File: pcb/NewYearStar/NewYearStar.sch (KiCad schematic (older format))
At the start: 22 parts, among them J1 Conn_01x03_Male, J2 Conn_01x02_Male, J3 Conn_01x02_Male, J4 Conn_01x02_Male, J5 Conn_01x02_Male

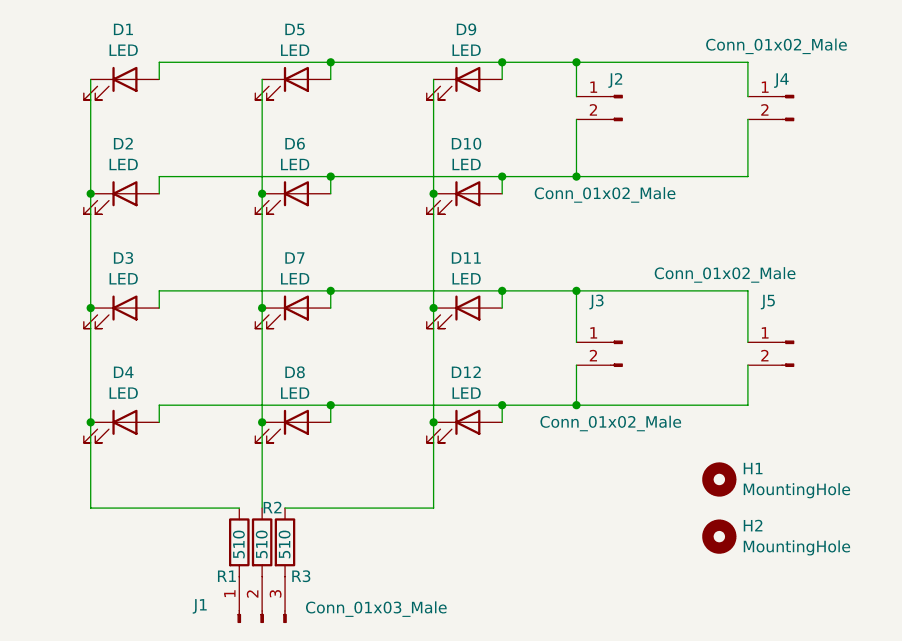
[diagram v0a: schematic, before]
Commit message: Add R for every LED
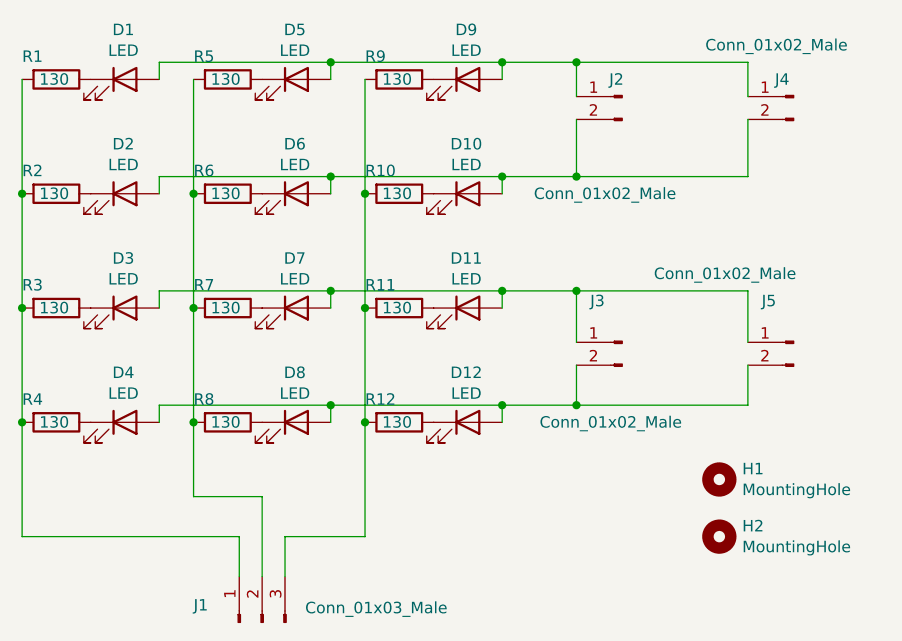
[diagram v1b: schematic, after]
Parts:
- added R10, R11, R12, R4, R5, R6, R7, R8, R9: 130, Resistor_SMD:R_0805_2012Metric_Pad1.20x1.40mm_HandSolder, symbol Device:R
- R1, R2, R3: value 510 -> 130
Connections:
- net at J1.1 (Pin_1), R1.2: now also R2.2, R3.2, R4.2
- net at J1.2 (Pin_2): now also R5.2, R6.2, R7.2, R8.2; no longer R2.2
- net at J1.3 (Pin_3): now also R10.2, R11.2, R12.2, R9.2; no longer R3.2
- new net: D1.1 (K), R1.1
- new net: D5.1 (K), R5.1
- new net: D9.1 (K), R9.1
- new net: D2.1 (K), R2.1
- new net: D6.1 (K), R6.1
- new net: D10.1 (K), R10.1
- new net: D3.1 (K), R3.1
- new net: D7.1 (K), R7.1
- new net: D11.1 (K), R11.1
- new net: D4.1 (K), R4.1
- new net: D8.1 (K), R8.1
- new net: D12.1 (K), R12.1
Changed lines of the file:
@@
 $EndComp
-Wire Wire Line
-	2750 2250 2750 2750
-Wire Wire Line
-	2750 2750 2750 3250
-Connection ~ 2750 2750
-Wire Wire Line
-	2750 3250 2750 3750
-Connection ~ 2750 3250
-Wire Wire Line
-	3500 2250 3500 2750
-Wire Wire Line
-	3500 2750 3500 3250
-Connection ~ 3500 2750
-Wire Wire Line
-	3500 3250 3500 3750
-Connection ~ 3500 3250
-Wire Wire Line
-	4250 2250 4250 2750
-Wire Wire Line
-	4250 2750 4250 3250
-Connection ~ 4250 2750
-Wire Wire Line
-	4250 3250 4250 3750
-Connection ~ 4250 3250
 Wire Wire Line
 	3050 2250 3050 2175
@@
 	0    -1   -1   0
 $EndComp
-Wire Wire Line
-	2750 3750 2750 4125
-Wire Wire Line
-	2750 4125 3400 4125
-Connection ~ 2750 3750
-Wire Wire Line
-	3600 4125 4250 4125
-Wire Wire Line
-	4250 4125 4250 3750
-Connection ~ 4250 3750
-Wire Wire Line
-	3500 4125 3500 3750
-Connection ~ 3500 3750
-$Comp
-L Device:R R3
-U 1 1 5FE1D08B
-P 3600 4275
-F 0 "R3" H 3625 4125 50  0000 L CNN
-F 1 "510" V 3600 4200 50  0000 L CNN
-F 2 "Resistor_SMD:R_0805_2012Metric_Pad1.20x1.40mm_HandSolder" V 3530 4275 50  0001 C CNN
-F 3 "~" H 3600 4275 50  0001 C CNN
-	1    3600 4275
-	1    0    0    -1
-$EndComp
-$Comp
-L Device:R R1
-U 1 1 5FE1D8DA
-P 3400 4275
-F 0 "R1" H 3300 4125 50  0000 L CNN
-F 1 "510" V 3400 4200 50  0000 L CNN
-F 2 "Resistor_SMD:R_0805_2012Metric_Pad1.20x1.40mm_HandSolder" V 3330 4275 50  0001 C CNN
-F 3 "~" H 3400 4275 50  0001 C CNN
-	1    3400 4275
-	1    0    0    -1
-$EndComp
-$Comp
-L Device:R R2
-U 1 1 5FE1DE75
-P 3500 4275
-F 0 "R2" H 3500 4425 50  0000 L CNN
-F 1 "510" V 3500 4200 50  0000 L CNN
-F 2 "Resistor_SMD:R_0805_2012Metric_Pad1.20x1.40mm_HandSolder" V 3430 4275 50  0001 C CNN
-F 3 "~" H 3500 4275 50  0001 C CNN
-	1    3500 4275
-	1    0    0    -1
-$EndComp
 $Comp
 L Connector:Conn_01x02_Male J2
@@
 Wire Wire Line
 	4875 3675 5625 3675
+$Comp
+L Device:R R1
+U 1 1 5FF39C8F
+P 2600 2250
+F 0 "R1" V 2500 2100 50  0000 L CNN
+F 1 "130" V 2600 2175 50  0000 L CNN
+F 2 "Resistor_SMD:R_0805_2012Metric_Pad1.20x1.40mm_HandSolder" V 2530 2250 50  0001 C CNN
+F 3 "~" H 2600 2250 50  0001 C CNN
+	1    2600 2250
+	0    1    1    0
+$EndComp
+$Comp
+L Device:R R2
+U 1 1 5FF3B6FB
+P 2600 2750
+F 0 "R2" V 2500 2600 50  0000 L CNN
+F 1 "130" V 2600 2675 50  0000 L CNN
+F 2 "Resistor_SMD:R_0805_2012Metric_Pad1.20x1.40mm_HandSolder" V 2530 2750 50  0001 C CNN
+F 3 "~" H 2600 2750 50  0001 C CNN
+	1    2600 2750
+	0    1    1    0
+$EndComp
+$Comp
+L Device:R R3
+U 1 1 5FF3BBF5
+P 2600 3250
+F 0 "R3" V 2500 3100 50  0000 L CNN
+F 1 "130" V 2600 3175 50  0000 L CNN
+F 2 "Resistor_SMD:R_0805_2012Metric_Pad1.20x1.40mm_HandSolder" V 2530 3250 50  0001 C CNN
+F 3 "~" H 2600 3250 50  0001 C CNN
+	1    2600 3250
+	0    1    1    0
+$EndComp
+$Comp
+L Device:R R4
+U 1 1 5FF3C028
+P 2600 3750
+F 0 "R4" V 2500 3600 50  0000 L CNN
+F 1 "130" V 2600 3675 50  0000 L CNN
+F 2 "Resistor_SMD:R_0805_2012Metric_Pad1.20x1.40mm_HandSolder" V 2530 3750 50  0001 C CNN
+F 3 "~" H 2600 3750 50  0001 C CNN
+	1    2600 3750
+	0    1    1    0
+$EndComp
+$Comp
+L Device:R R5
+U 1 1 5FF3C63D
+P 3350 2250
+F 0 "R5" V 3250 2100 50  0000 L CNN
+F 1 "130" V 3350 2175 50  0000 L CNN
+F 2 "Resistor_SMD:R_0805_2012Metric_Pad1.20x1.40mm_HandSolder" V 3280 2250 50  0001 C CNN
+F 3 "~" H 3350 2250 50  0001 C CNN
+	1    3350 2250
+	0    1    1    0
+$EndComp
+$Comp
+L Device:R R6
+U 1 1 5FF3CA5F
+P 3350 2750
+F 0 "R6" V 3250 2600 50  0000 L CNN
+F 1 "130" V 3350 2675 50  0000 L CNN
+F 2 "Resistor_SMD:R_0805_2012Metric_Pad1.20x1.40mm_HandSolder" V 3280 2750 50  0001 C CNN
+F 3 "~" H 3350 2750 50  0001 C CNN
+	1    3350 2750
+	0    1    1    0
+$EndComp
+$Comp
+L Device:R R7
+U 1 1 5FF3CF05
+P 3350 3250
+F 0 "R7" V 3250 3100 50  0000 L CNN
+F 1 "130" V 3350 3175 50  0000 L CNN
+F 2 "Resistor_SMD:R_0805_2012Metric_Pad1.20x1.40mm_HandSolder" V 3280 3250 50  0001 C CNN
+F 3 "~" H 3350 3250 50  0001 C CNN
+	1    3350 3250
+	0    1    1    0
+$EndComp
+$Comp
+L Device:R R8
+U 1 1 5FF3D41F
+P 3350 3750
+F 0 "R8" V 3250 3600 50  0000 L CNN
+F 1 "130" V 3350 3675 50  0000 L CNN
+F 2 "Resistor_SMD:R_0805_2012Metric_Pad1.20x1.40mm_HandSolder" V 3280 3750 50  0001 C CNN
+F 3 "~" H 3350 3750 50  0001 C CNN
+	1    3350 3750
+	0    1    1    0
+$EndComp
+$Comp
+L Device:R R9
+U 1 1 5FF3DA83
+P 4100 2250
+F 0 "R9" V 4000 2100 50  0000 L CNN
+F 1 "130" V 4100 2175 50  0000 L CNN
+F 2 "Resistor_SMD:R_0805_2012Metric_Pad1.20x1.40mm_HandSolder" V 4030 2250 50  0001 C CNN
+F 3 "~" H 4100 2250 50  0001 C CNN
+	1    4100 2250
+	0    1    1    0
+$EndComp
+$Comp
+L Device:R R10
+U 1 1 5FF3DE6D
+P 4100 2750
+F 0 "R10" V 4000 2600 50  0000 L CNN
+F 1 "130" V 4100 2675 50  0000 L CNN
+F 2 "Resistor_SMD:R_0805_2012Metric_Pad1.20x1.40mm_HandSolder" V 4030 2750 50  0001 C CNN
+F 3 "~" H 4100 2750 50  0001 C CNN
+	1    4100 2750
+	0    1    1    0
+$EndComp
+$Comp
+L Device:R R11
+U 1 1 5FF3E26B
+P 4100 3250
+F 0 "R11" V 4000 3100 50  0000 L CNN
+F 1 "130" V 4100 3175 50  0000 L CNN
+F 2 "Resistor_SMD:R_0805_2012Metric_Pad1.20x1.40mm_HandSolder" V 4030 3250 50  0001 C CNN
+F 3 "~" H 4100 3250 50  0001 C CNN
+	1    4100 3250
+	0    1    1    0
+$EndComp
+$Comp
+L Device:R R12
+U 1 1 5FF3E5AF
+P 4100 3750
+F 0 "R12" V 4000 3600 50  0000 L CNN
+F 1 "130" V 4100 3675 50  0000 L CNN
+F 2 "Resistor_SMD:R_0805_2012Metric_Pad1.20x1.40mm_HandSolder" V 4030 3750 50  0001 C CNN
+F 3 "~" H 4100 3750 50  0001 C CNN
+	1    4100 3750
+	0    1    1    0
+$EndComp
+Wire Wire Line
+	3950 2250 3950 2750
+Wire Wire Line
+	3950 2750 3950 3250
+Connection ~ 3950 2750
+Wire Wire Line
+	3950 3250 3950 3750
+Connection ~ 3950 3250
+Wire Wire Line
+	3950 3750 3950 4250
+Wire Wire Line
+	3950 4250 3600 4250
+Wire Wire Line
+	3600 4250 3600 4425
+Connection ~ 3950 3750
+Wire Wire Line
+	3200 3250 3200 3750
+Connection ~ 3200 3250
+Wire Wire Line
+	3200 3750 3200 4075
+Wire Wire Line
+	3200 4075 3500 4075
+Wire Wire Line
+	3500 4075 3500 4425
+Connection ~ 3200 3750
+Wire Wire Line
+	2450 2250 2450 2750
+Wire Wire Line
+	2450 2750 2450 3250
+Connection ~ 2450 2750
+Wire Wire Line
+	2450 3250 2450 3750
+Connection ~ 2450 3250
+Wire Wire Line
+	2450 3750 2450 4250
+Wire Wire Line
+	2450 4250 3400 4250
+Wire Wire Line
+	3400 4250 3400 4425
+Connection ~ 2450 3750
+Wire Wire Line
+	3200 2250 3200 2750
+Connection ~ 3200 2750
+Wire Wire Line
+	3200 2750 3200 3250
 $EndSCHEMATC
